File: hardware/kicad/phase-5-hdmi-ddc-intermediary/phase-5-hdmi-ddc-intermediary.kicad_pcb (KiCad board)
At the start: 4 copper layers, 110 x 65 mm, 23 parts, among them J1 HDMI_SOURCE, J2 HDMI_MONITOR, J3 PI_HOST_CTRL, Q1 2N7002, U1 TCA4307DGKR, U2 PCA9306DCTR, U3 TPS2113APWR

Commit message: Phase 5 WIP
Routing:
- net +3V3_PI: track 122.3 -> 84.8 mm, vias 2 -> 3
- net SDA_DDC: track 127.2 -> 105.0 mm, vias 2 -> 4
- net GND: track 0.00 -> 7.87 mm, vias 0 -> 3
- net +5V_PI: track 266.8 -> 261.2 mm
- net SDA_SRC: track 63.8 -> 67.8 mm
- net HDMI_5V_SRC: track 73.9 -> 76.9 mm
- net PI_SDA: track 72.3 -> 70.0 mm, vias 2 -> 1
- net PIN18_STAT: track 48.0 -> 47.0 mm
- net HDMI_5V_MON: track 70.7 -> 71.3 mm, vias 0 -> 5
- net SCL_SRC: track 53.9 -> 54.5 mm
- net MON_5V_DISABLE: track 51.2 -> 50.7 mm, vias 2 -> 3
- net SCL_DDC: track 115.7 -> 115.2 mm, vias 2 -> 4
- net HPD_MON_SRC: track 96.7 -> 97.2 mm, vias 0 -> 3
- net PI_SCL: track 64.0 -> 64.2 mm, vias 2 -> 1
- net HPD_SENSE: track 45.7 -> 45.8 mm, vias 2 -> 3

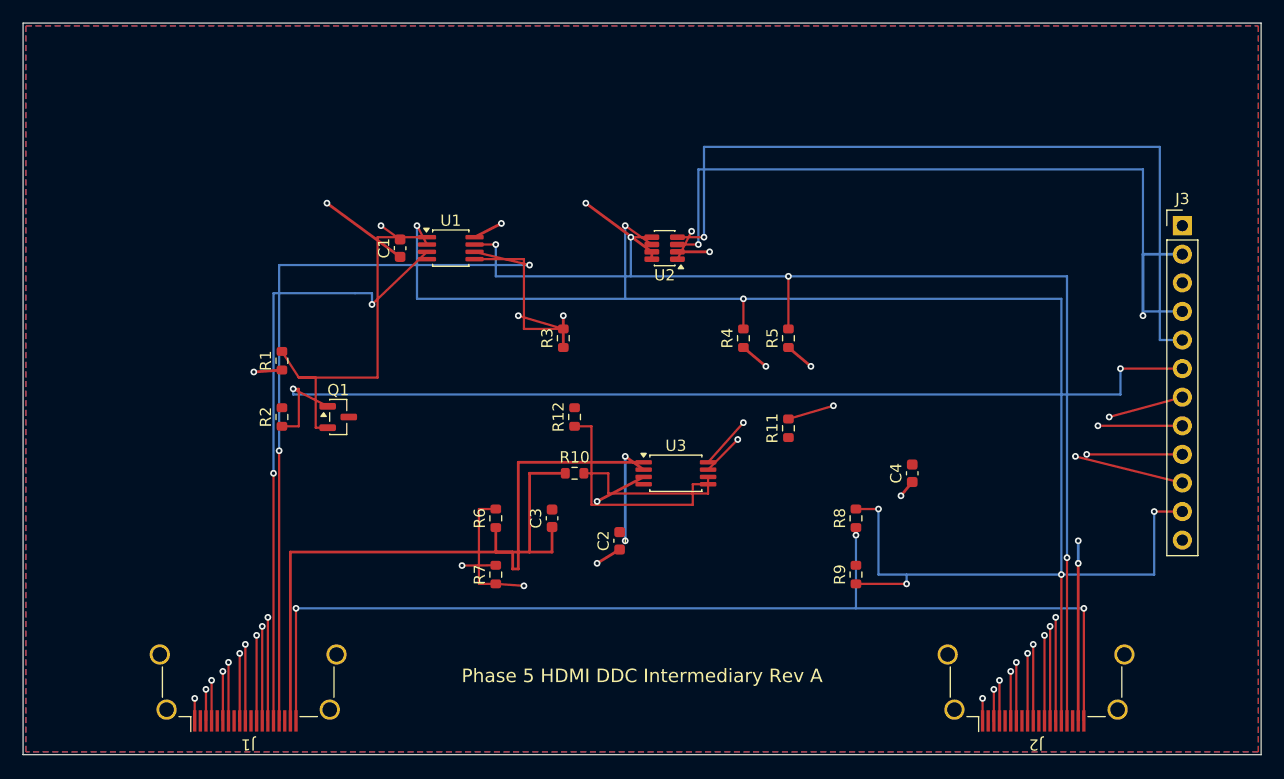
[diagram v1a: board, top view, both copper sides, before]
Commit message: Update phase 5 documents and schematics
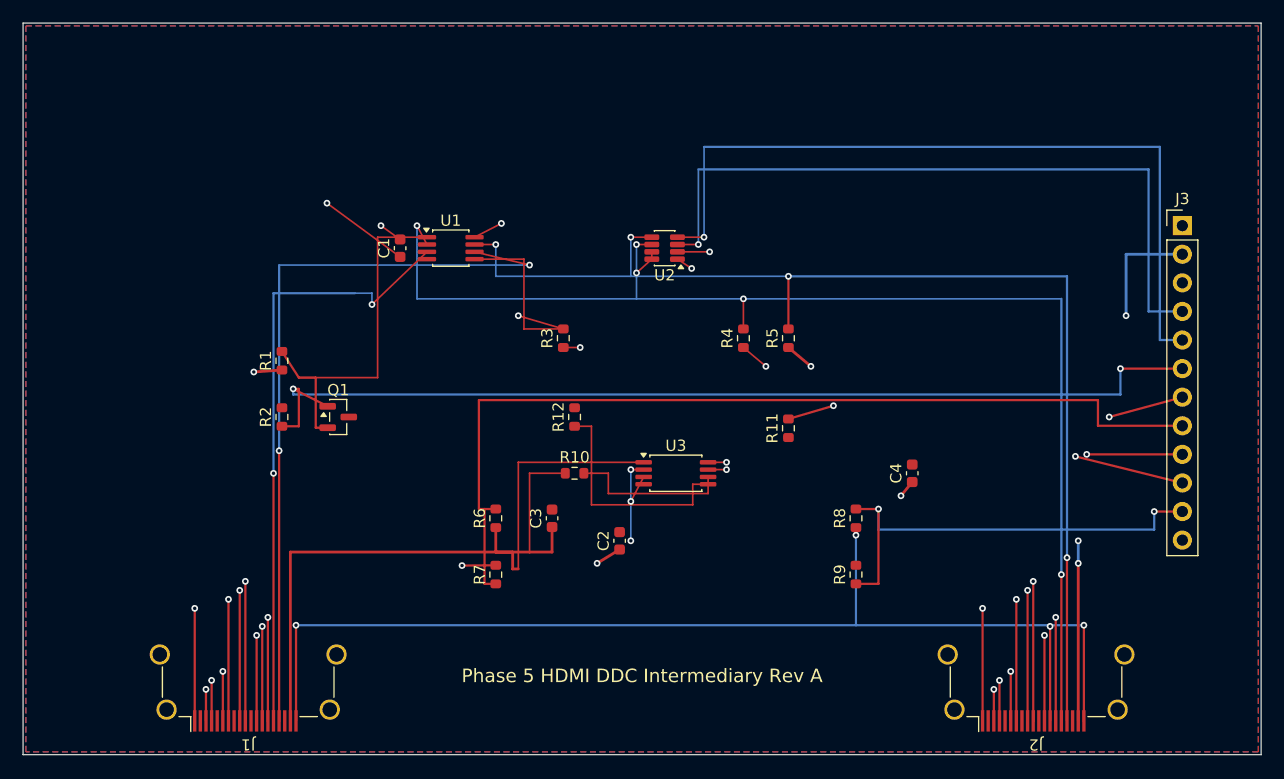
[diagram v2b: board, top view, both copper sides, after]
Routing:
- net TMDS2_P: track 74.0 -> 90.0 mm
- net TMDSCLK_P: track 83.6 -> 94.8 mm
- net TMDS0_N: track 82.0 -> 93.2 mm
- net TMDS0_P: track 80.4 -> 91.6 mm
- net HPD_SENSE: track 45.8 -> 41.1 mm, vias 3 -> 2
- net SRC_5V_SENSE: track 87.9 -> 83.6 mm, vias 2 -> 0
- net PIN18_STAT: track 47.0 -> 43.0 mm
- net SCL_DDC: track 115.2 -> 112.0 mm
- net HDMI_5V_MON: track 71.3 -> 68.8 mm
- net MON_5V_DISABLE: track 50.7 -> 52.2 mm
- net HPD_MON_SRC: track 97.2 -> 95.7 mm
- net +3V3_PI: track 84.8 -> 83.3 mm
- net +5V_PI: track 261.2 -> 259.8 mm
- net GND: track 7.87 -> 6.60 mm
